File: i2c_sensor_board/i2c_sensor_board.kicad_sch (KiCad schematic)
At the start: 3 parts, among them J1 Conn_01x04_Pin, J2 Conn_01x04_Pin, U1 STM32G030K8Tx

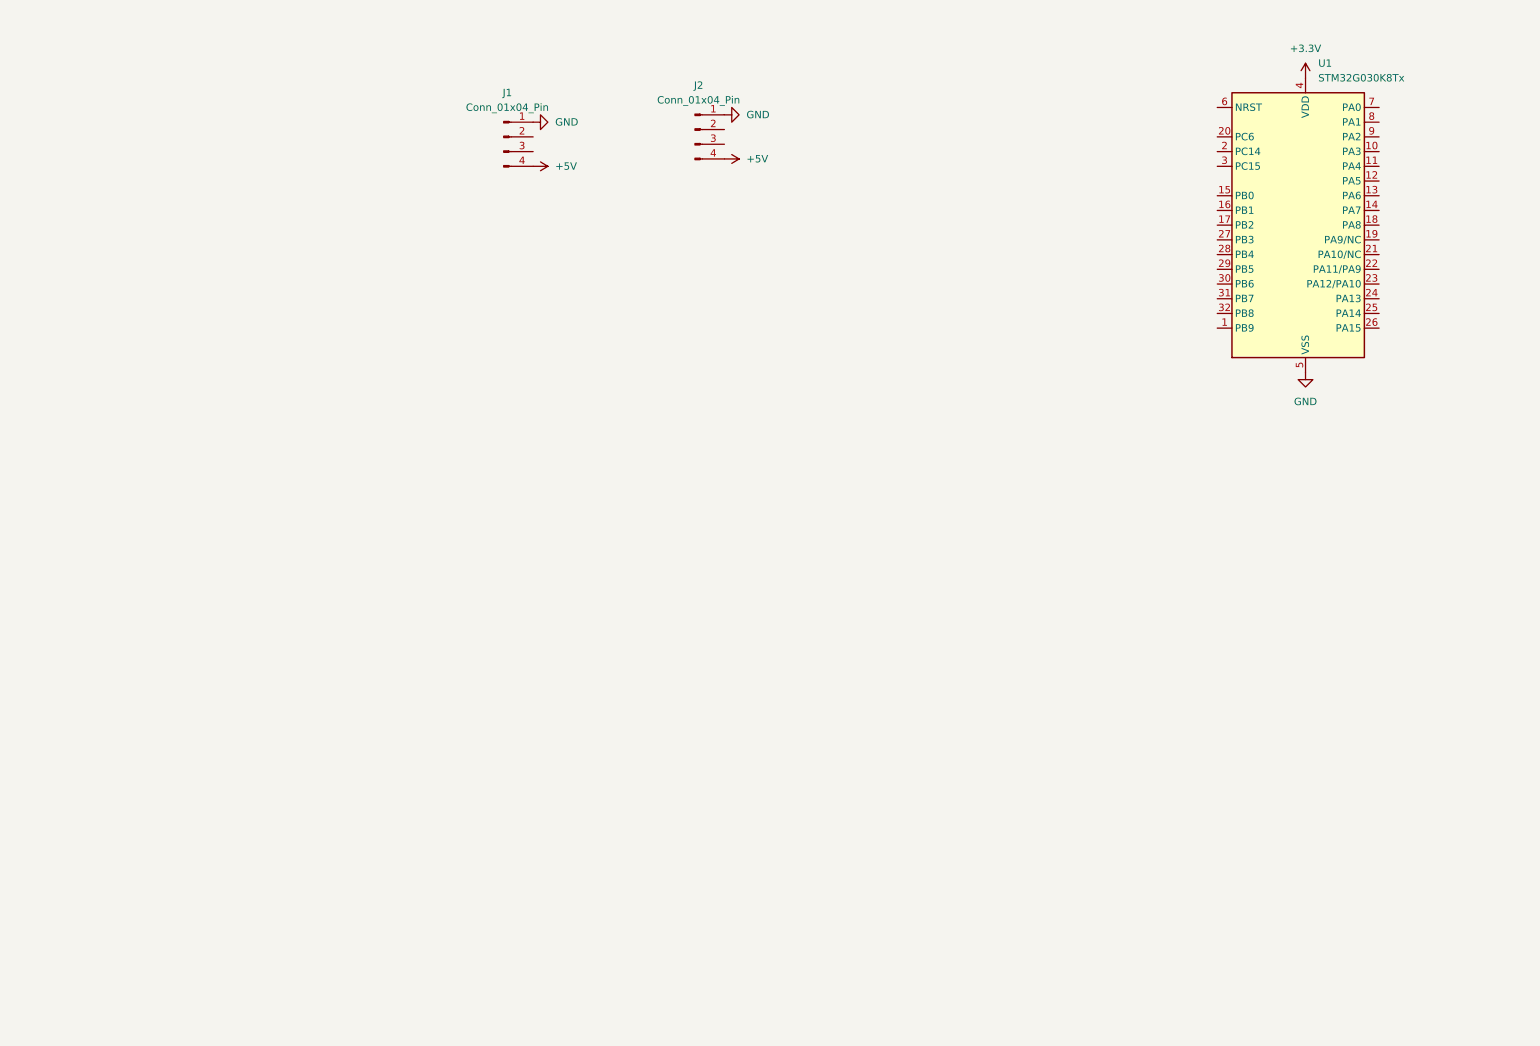
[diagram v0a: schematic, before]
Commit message: Add I2C boards
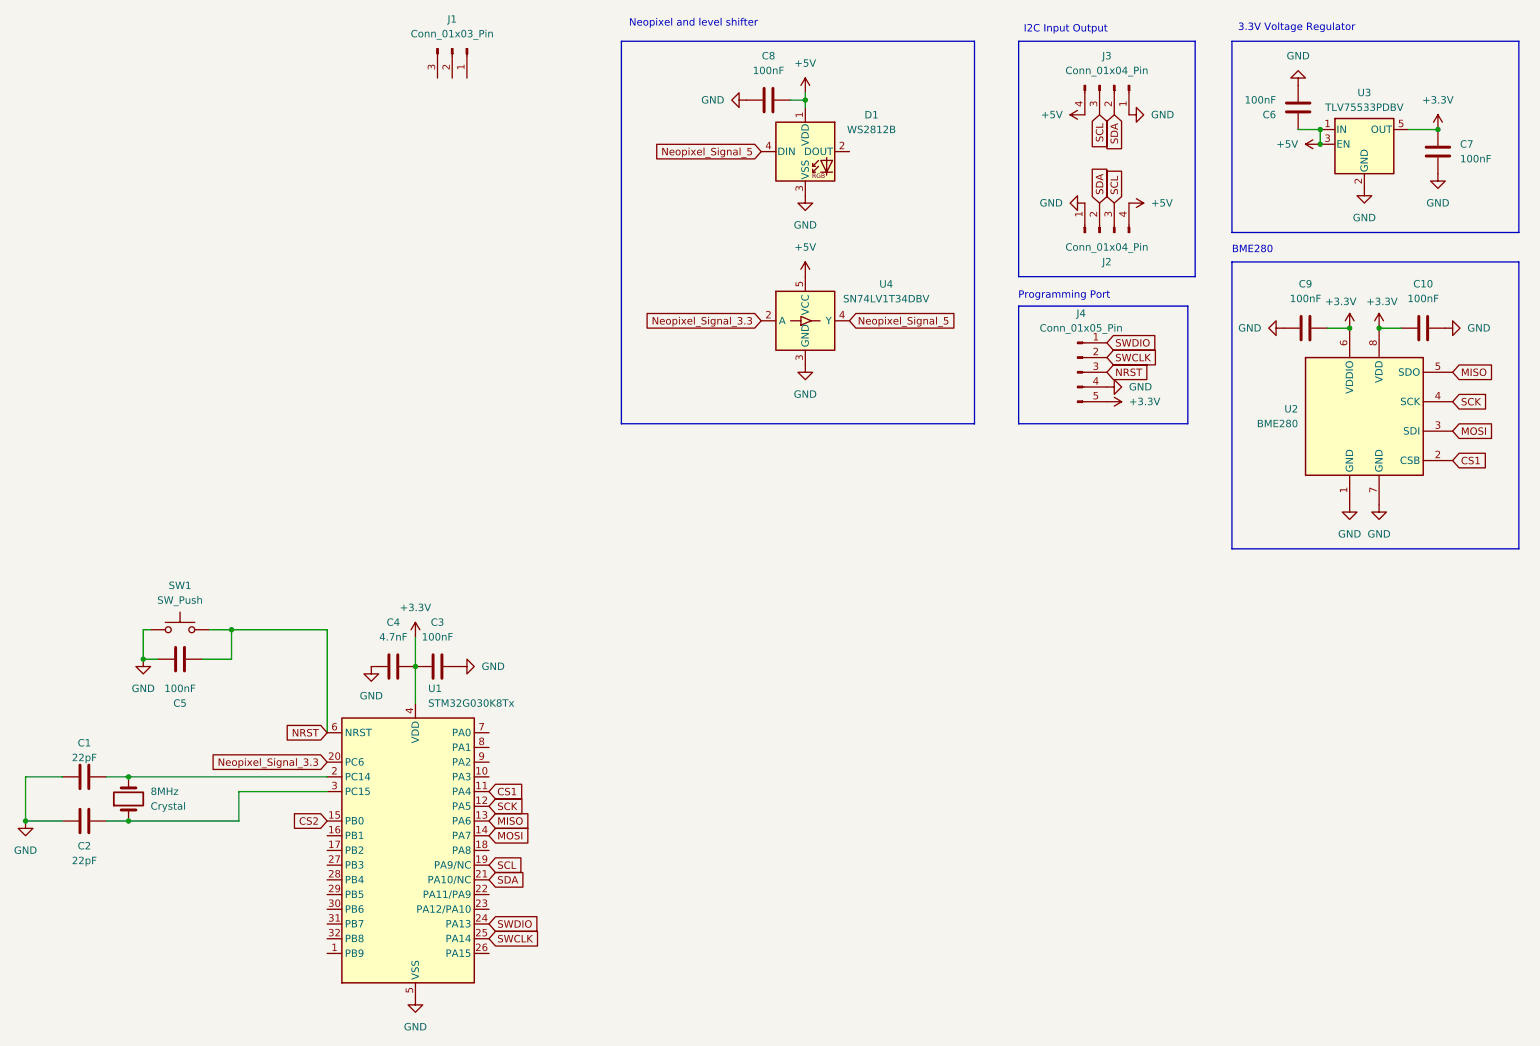
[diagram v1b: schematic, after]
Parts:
- removed J1: Conn_01x04_Pin, symbol Connector:Conn_01x04_Pin
- added 8MHz: Crystal, Crystal:Crystal_HC49-U_Vertical, symbol Device:Crystal
- added C1, C2: 22pF, Capacitor_SMD:C_0603_1608Metric_Pad1.08x0.95mm_HandSolder, symbol Device:C
- added C10, C9: 100nF, symbol Device:C
- added C3, C5, C6, C7, C8: 100nF, Capacitor_SMD:C_0603_1608Metric_Pad1.08x0.95mm_HandSolder, symbol Device:C
- added C4: 4.7nF, Capacitor_SMD:C_0603_1608Metric_Pad1.08x0.95mm_HandSolder, symbol Device:C
- added D1: WS2812B, LED_SMD:LED_WS2812B_PLCC4_5.0x5.0mm_P3.2mm, symbol LED:WS2812B
- added J1: Conn_01x03_Pin, Connector_JST:JST_XH_B3B-XH-AM_1x03_P2.50mm_Vertical, symbol Connector:Conn_01x03_Pin
- added J3: Conn_01x04_Pin, Connector_JST:JST_XH_B4B-XH-AM_1x04_P2.50mm_Vertical, symbol Connector:Conn_01x04_Pin
- added J4: Conn_01x05_Pin, Connector_PinHeader_2.54mm:PinHeader_1x05_P2.54mm_Vertical, symbol Connector:Conn_01x05_Pin
- added SW1: SW_Push, Button_Switch_SMD:SW_SPST_PTS810, symbol Switch:SW_Push
- added U2: BME280, Package_LGA:Bosch_LGA-8_2.5x2.5mm_P0.65mm_ClockwisePinNumbering, symbol Sensor:BME280
- added U3: TLV75533PDBV, Package_TO_SOT_SMD:SOT-23-5, symbol Regulator_Linear:TLV75533PDBV
- added U4: SN74LV1T34DBV, Package_TO_SOT_SMD:SOT-23-5, symbol Logic_LevelTranslator:SN74LV1T34DBV
- J2: footprint (none) -> Connector_JST:JST_XH_B4B-XH-AM_1x04_P2.50mm_Vertical
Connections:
- net +3.3V: now also C10.2, C3.1, C4.2, C7.1, C9.1, J4.5 (Pin_5), U2.6 (VDDIO), U2.8 (VDD), U3.5 (OUT)
- net +5V: now also C6.1, C8.2, D1.1 (VDD), J3.4 (Pin_4), U3.1 (IN), U3.3 (EN), U4.5 (VCC)
- net GND: now also C1.1, C10.1, C2.1, C3.2, C4.1, C5.1, C6.2, C7.2, C8.1, C9.2, D1.3 (VSS), J3.1 (Pin_1), J4.4 (Pin_4), SW1.1, U2.1 (GND), U2.7 (GND), U3.2 (GND), U4.3 (GND)
- net SDA: now reaches J2.2 (Pin_2)
- net SDA: now also U1.21 (PA10/NC), J3.2 (Pin_2)
- net SCL: now reaches J2.3 (Pin_3)
- net SCL: now also U1.19 (PA9/NC), J3.3 (Pin_3)
- net CS1: now reaches U1.11 (PA4)
- net CS1: now also U2.2 (CSB)
- net SCK: now reaches U1.12 (PA5)
- net SCK: now also U2.4 (SCK)
- net MISO: now reaches U1.13 (PA6)
- net MISO: now also U2.5 (SDO)
- net MOSI: now reaches U1.14 (PA7)
- net MOSI: now also U2.3 (SDI)
- net CS2: now reaches U1.15 (PB0)
- net at U1.2 (PC14): now also 8MHz.2, C1.2
- net Neopixel_Signal_3.3: now reaches U1.20 (PC6)
- net Neopixel_Signal_3.3: now also U4.2 (A)
- net SWDIO: now reaches U1.24 (PA13)
- net SWDIO: now also J4.1 (Pin_1)
- net SWCLK: now reaches U1.25 (PA14)
- net SWCLK: now also J4.2 (Pin_2)
- net at U1.3 (PC15): now also 8MHz.1, C2.2
- net NRST: now reaches U1.6 (NRST)
- net NRST: now also C5.2, J4.3 (Pin_3), SW1.2
- new net Neopixel_Signal_5: D1.4 (DIN), U4.4 (Y)
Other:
- note added: "3.3V Voltage Regulator"
- note added: "BME280"
- note added: "I2C Input Output"
- note added: "Neopixel and level shifter"
- note added: "Programming Port"

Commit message: Lots of changes
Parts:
- added H1, H2, H3, H4: MountingHole_Pad, MountingHole:MountingHole_3.2mm_M3_DIN965_Pad, symbol Mechanical:MountingHole_Pad
- added J5: Conn_01x05_Pin, Connector_JST:JST_XH_B5B-XH-AM_1x05_P2.50mm_Vertical, symbol Connector:Conn_01x05_Pin
- added J6: Conn_01x02_Pin, Connector_JST:JST_XH_B2B-XH-AM_1x02_P2.50mm_Vertical, symbol Connector:Conn_01x02_Pin
- added J7: Conn_02x05_Counter_Clockwise, Connector_PinHeader_2.54mm:PinHeader_2x05_P2.54mm_Vertical, symbol Connector_Generic:Conn_02x05_Counter_Clockwise
- added R1: 20K, Resistor_SMD:R_0603_1608Metric_Pad0.98x0.95mm_HandSolder, symbol Device:R
- added U5: TMCS1100A2QDR, SOIC8_D_TEX, symbol 2024-10-24_21-10-15:TMCS1100A2QDR
- added U6: LM4030-2.5, Package_TO_SOT_SMD:SOT-23-5, symbol Reference_Voltage:LM4030-2.5
- C10, C9: footprint (none) -> Capacitor_SMD:C_0603_1608Metric_Pad1.08x0.95mm_HandSolder
- J4: footprint Connector_PinHeader_2.54mm:PinHeader_1x05_P2.54mm_Vertical -> Connector_PinSocket_2.54mm:PinSocket_1x05_P2.54mm_Vertical
- renumbered 8MHz to 8MHz1
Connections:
- net +3.3V: now also U5.8 (VS)
- net +5V: now also J1.3 (Pin_3), J6.2 (Pin_2), J7.2 (Pin_2), R1.1, U5.3 (IN-), U5.4 (IN-); no longer J2.4 (Pin_4), J3.4 (Pin_4)
- net CS2: now also J5.2 (Pin_2)
- net GND: now also J1.1 (Pin_1), H1.1, H2.1, H3.1, H4.1, J5.1 (Pin_1), J6.1 (Pin_1), J7.1 (Pin_1), U5.5 (GND), U6.5 (A)
- net MISO: now also J5.5 (Pin_5)
- net MOSI: now also J5.4 (Pin_4)
- net SCK: now also J5.3 (Pin_3)
- net GPIO_SENS: now reaches J1.2 (Pin_2)
- net GPIO_SENS: now also U1.7 (PA0)
- net CurrentAnalog: now reaches U1.16 (PB1)
- net CurrentAnalog: now also U5.7 (VOUT)
- net PA11/PA9: now reaches U1.22 (PA11/PA9)
- net PA11/PA9: now also J7.9 (Pin_9)
- net PA12/PA10: now reaches U1.23 (PA12/PA10)
- net PA12/PA10: now also J7.10 (Pin_10)
- net PB3: now reaches U1.27 (PB3)
- net PB3: now also J7.8 (Pin_8)
- net PB4: now reaches U1.28 (PB4)
- net PB4: now also J7.7 (Pin_7)
- net PB5: now reaches U1.29 (PB5)
- net PB5: now also J7.6 (Pin_6)
- net PB6: now reaches U1.30 (PB6)
- net PB6: now also J7.5 (Pin_5)
- net PB7: now reaches U1.31 (PB7)
- net PB7: now also J7.4 (Pin_4)
- net PB8: now reaches U1.32 (PB8)
- net PB8: now also J7.3 (Pin_3)
- new net: R1.2, U5.6 (VREF), U6.4 (K)
- new net Input 5V: J2.4 (Pin_4), J3.4 (Pin_4), U5.1 (IN+), U5.2 (IN+)
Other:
- note added: "5V Aux Power Port"
- note added: "SPI Port"
- note added: "Sensor Port"
- moved on the sheet: J1
